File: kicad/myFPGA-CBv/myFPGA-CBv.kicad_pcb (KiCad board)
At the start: 2 copper layers, 50 x 140 mm, 52 parts, among them J1 Conn_01x04, J10 Conn_01x04, J2 Conn_01x04, J3 Conn_01x04, J4 Conn_01x04, J5 Conn_01x02, J6 Conn_01x02, J7 Conn_01x04, J8 Conn_01x04, J9 Conn_01x04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

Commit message: more kicad layouts 2.
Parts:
- moved U1 204.1 mm to (76.5, 128.9)
- moved C2 181.1 mm to (126.0, 154.1), turned to 90 degrees
- moved C4 176.5 mm to (129.3, 154.1), turned to 90 degrees
- moved R4 163.9 mm to (82.9, 98.4), turned to -90 degrees
- moved U2 161.6 mm to (79.0, 97.2)
- moved U4 158.1 mm to (91.8, 109.8)
- moved U3 156.4 mm to (85.4, 103.5)
- moved D4 155.7 mm to (79.0, 99.7)
- moved U5 153.3 mm to (98.1, 116.2)
- moved D3 152.6 mm to (85.4, 106.0)
- moved R3 152.3 mm to (89.2, 104.8), turned to -90 degrees
- moved D2 150.2 mm to (91.8, 112.4)
- moved D1 148.7 mm to (98.1, 118.7)
- moved R2 148.7 mm to (95.6, 111.1), turned to -90 degrees
- moved R1 145.8 mm to (101.9, 117.5), turned to -90 degrees
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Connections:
- net Net-(J2-Pin_1) renamed /s_0
- net Net-(J2-Pin_2) renamed /s_1
- net Net-(J2-Pin_3) renamed /s_2
- net Net-(J2-Pin_4) renamed /s_3
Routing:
- net bus_3: track 0.00 -> 146.3 mm
- net bus_2: track 0.00 -> 143.2 mm
- net bus_1: track 0.00 -> 140.0 mm
- net bus_0: track 0.00 -> 136.9 mm
- net prio_0: track 0.00 -> 132.0 mm
- net prio_1: track 0.00 -> 128.7 mm
- net /s_0: track 0.00 -> 85.5 mm, vias 0 -> 2
- net /s_3: track 0.00 -> 82.5 mm, vias 0 -> 2
- net /s_1: track 0.00 -> 82.2 mm, vias 0 -> 2
- net /s_2: track 0.00 -> 79.3 mm, vias 0 -> 2
- net GND: track 0.00 -> 63.5 mm, vias 0 -> 14
- net +3.3VP: track 0.00 -> 10.7 mm, vias 0 -> 8
- net xp_7: track 0.00 -> 3.97 mm
- net xp_0: track 0.00 -> 3.97 mm
- net xp_5: track 0.00 -> 3.95 mm
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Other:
- board size 50 x 140 mm -> 90 x 140 mm

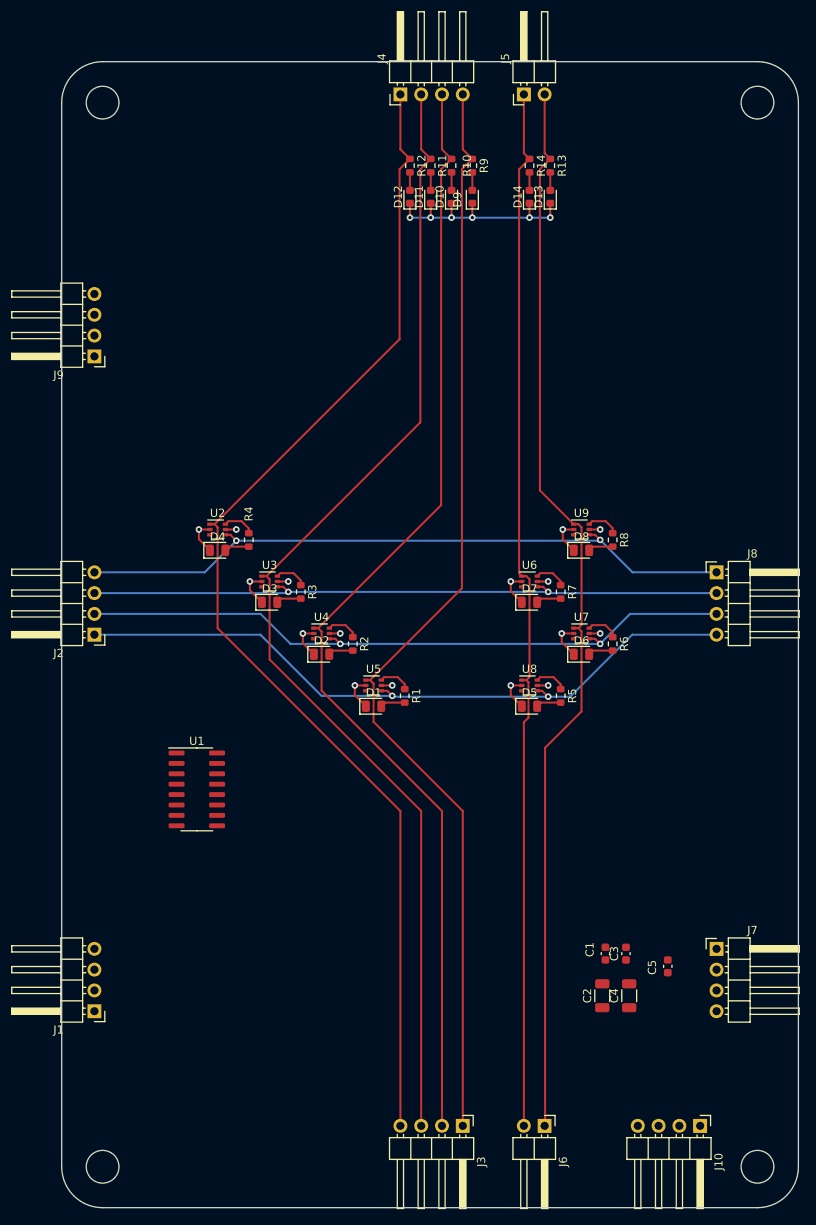
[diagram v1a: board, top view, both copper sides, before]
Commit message: found more bugs
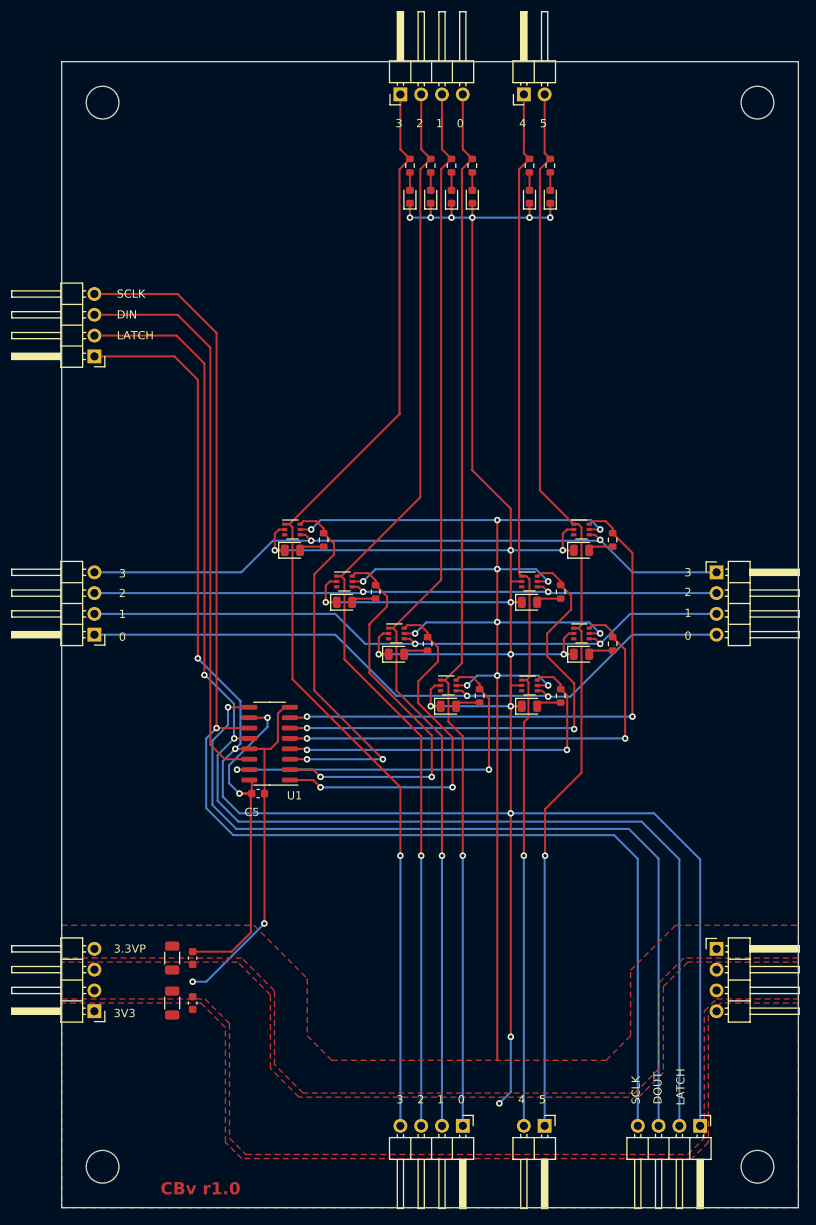
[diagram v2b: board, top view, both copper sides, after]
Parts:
- added G***: LOGO, LOGO, B.Cu at (83.5, 75.3)
- moved C4 55.8 mm to (73.5, 155.0)
- moved C5 54.3 mm to (84.0, 129.4), turned to 0 degrees
- moved C3 53.3 mm to (76.0, 155.0)
- moved C2 52.7 mm to (73.5, 149.5), turned to -90 degrees
- moved C1 50.4 mm to (76.0, 149.5), turned to -90 degrees
- moved U1 10.5 mm to (85.4, 123.3), turned to 180 degrees
- moved D1 9.14 mm to (107.2, 118.7)
- moved D2 9.14 mm to (100.9, 112.4)
- moved D4 9.14 mm to (88.2, 99.7)
- moved R1 9.14 mm to (111.1, 117.5)
- moved R3 9.14 mm to (98.4, 104.8)
- moved R4 9.14 mm to (92.0, 98.4)
- moved U2 9.14 mm to (88.2, 97.2)
- moved U4 9.14 mm to (100.9, 109.8)
- moved U5 9.14 mm to (107.2, 116.2)
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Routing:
- net GND: track 63.5 -> 471.0 mm, vias 14 -> 23
- net +3.3VP: track 10.7 -> 215.0 mm, vias 8 -> 14
- net SCLK: track 0.00 -> 167.4 mm, vias 0 -> 1
- net LATCH: track 0.00 -> 164.5 mm, vias 0 -> 2
- net MISO: track 0.00 -> 105.2 mm, vias 0 -> 1
- net MOSI: track 0.00 -> 69.8 mm
- net xp_7: track 3.97 -> 69.3 mm, vias 0 -> 2
- net xp_6: track 3.90 -> 59.4 mm, vias 0 -> 2
- net xp_5: track 3.95 -> 57.9 mm, vias 0 -> 2
- net xp_2: track 3.95 -> 49.7 mm, vias 0 -> 2
- net xp_3: track 3.95 -> 47.9 mm, vias 0 -> 2
- net xp_0: track 3.97 -> 46.6 mm, vias 0 -> 2
- net xp_1: track 3.95 -> 45.8 mm, vias 0 -> 2
- net xp_4: track 3.95 -> 45.6 mm, vias 0 -> 2
- net bus_1: track 140.0 -> 132.5 mm, vias 0 -> 1
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- added copper zone on F.Cu, net +3.3VP
- added copper zone on F.Cu, net +3V3
- added copper zone on F.Cu, net GND
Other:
- outline, holes or cut-outs redrawn
- board text added: "0"
- board text added: "1"
- board text added: "2"
- board text added: "3"
- board text added: "3.3VP"
- board text added: "3V3"
- board text added: "4"
- board text added: "5"
- board text added: "CBv r1.0"
- board text added: "DIN"
- board text added: "DOUT"
- board text added: "LATCH"
- board text added: "SCLK"
